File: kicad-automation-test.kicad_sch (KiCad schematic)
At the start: 7 parts, among them J1 Input

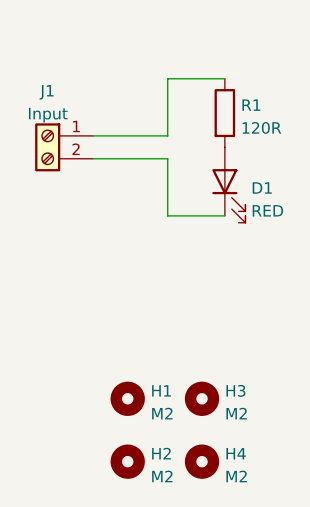
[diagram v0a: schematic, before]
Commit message: Added schematic label
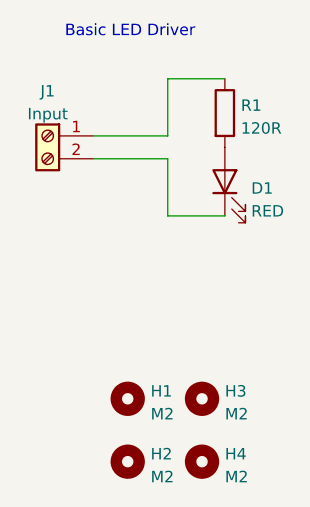
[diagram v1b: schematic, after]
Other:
- note added: "Basic LED Driver"
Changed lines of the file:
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@@
     (stroke (width 0) (type default) (color 0 0 0 0))
+  )
+  (text "Basic LED Driver" (at 132.715 74.93 0)
+    (effects (font (size 1.27 1.27)) (justify left bottom))
   )
   (symbol (lib_id "Mechanical:MountingHole") (at 147.955 114.935 0) (unit 1)
